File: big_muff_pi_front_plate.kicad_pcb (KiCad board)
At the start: 2 copper layers, 80 x 100 mm, 14 parts

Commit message: Finalized estetics.
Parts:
- added H11: MountingHole, MountingHole:MountingHole_3.2mm_M3_DIN965_Pad_TopBottom, F.Cu at (90.0, 145.0)
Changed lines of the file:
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@@
+		(embedded_fonts no)
+	)
+	(footprint "MountingHole:MountingHole_3.2mm_M3_DIN965_Pad_TopBottom"
+		(layer "F.Cu")
+		(at 90 145)
+		(descr "Mounting Hole 3.2mm, M3, DIN965")
+		(tags "mounting hole 3.2mm m3 din965")
+		(property "Reference" "H11"
+			(at 0 -3.8 0)
+			(layer "F.SilkS")
+			(hide yes)
+			(effects
+				(font
+					(size 1 1)
+					(thickness 0.15)
+				)
+			)
+		)
+		(property "Value" "MountingHole"
+			(at 0 3.8 0)
+			(layer "F.Fab")
+			(effects
+				(font
+					(size 1 1)
+					(thickness 0.15)
+				)
+			)
+		)
+		(property "Datasheet" ""
+			(at 0 0 0)
+			(unlocked yes)
+			(layer "F.Fab")
+			(hide yes)
+			(effects
+				(font
+					(size 1.27 1.27)
+					(thickness 0.15)
+				)
+			)
+		)
+		(property "Description" ""
+			(at 0 0 0)
+			(unlocked yes)
+			(layer "F.Fab")
+			(hide yes)
+			(effects
+				(font
+					(size 1.27 1.27)
+					(thickness 0.15)
+				)
+			)
+		)
+		(property ki_fp_filters "MountingHole*")
+		(sheetname "/")
+		(sheetfile "big_muff_pi_front_plate.kicad_sch")
+		(attr exclude_from_pos_files)
+		(fp_circle
+			(center 0 0)
+			(end 2.8 0)
+			(stroke
+				(width 0.15)
+				(type solid)
+			)
+			(fill no)
+			(layer "Cmts.User")
+		)
+		(fp_circle
+			(center 0 0)
+			(end 3.05 0)
+			(stroke
+				(width 0.05)
+				(type solid)
+			)
+			(fill no)
+			(layer "F.CrtYd")
+		)
+		(fp_text user "${REFERENCE}"
+			(at 0 0 0)
+			(layer "F.Fab")
+			(effects
+				(font
+					(size 1 1)
+					(thickness 0.15)
+				)
+			)
+		)
+		(pad "1" thru_hole circle
+			(at 0 0)
+			(size 3.6 3.6)
+			(drill 3.2)
+			(layers "*.Cu" "*.Mask")
+			(remove_unused_layers no)
+		)
+		(pad "1" connect circle
+			(at 0 0)
+			(size 5.6 5.6)
+			(layers "F.Cu" "F.Mask")
+		)
+		(pad "1" connect circle
+			(at 0 0)
+			(size 5.6 5.6)
+			(layers "B.Cu" "B.Mask")
+		)
 		(embedded_fonts no)
 	)

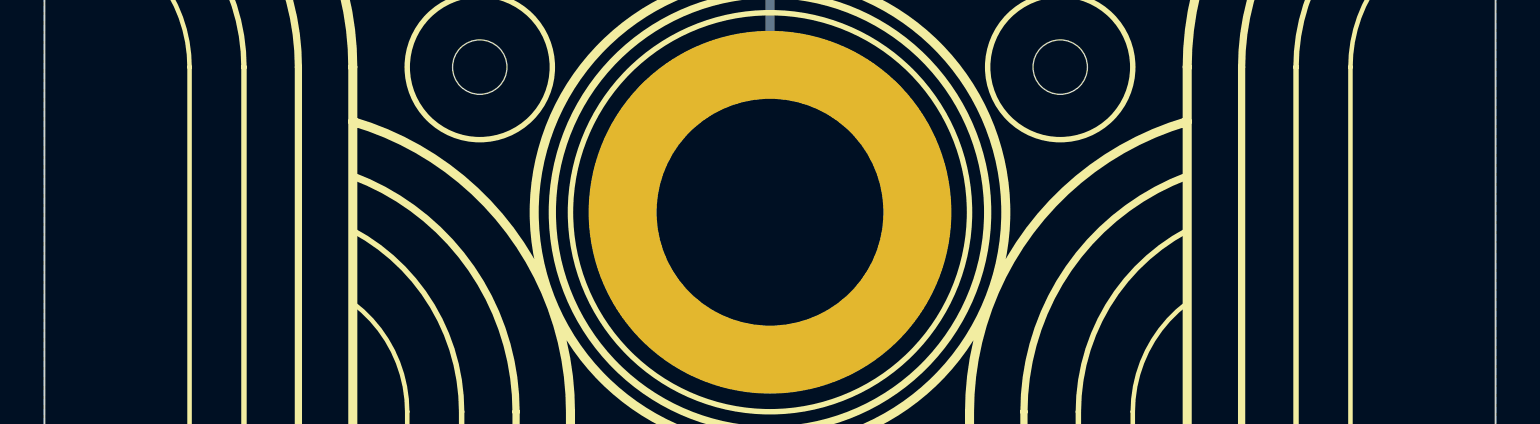
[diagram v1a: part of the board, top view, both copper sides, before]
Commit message: Added input labels.
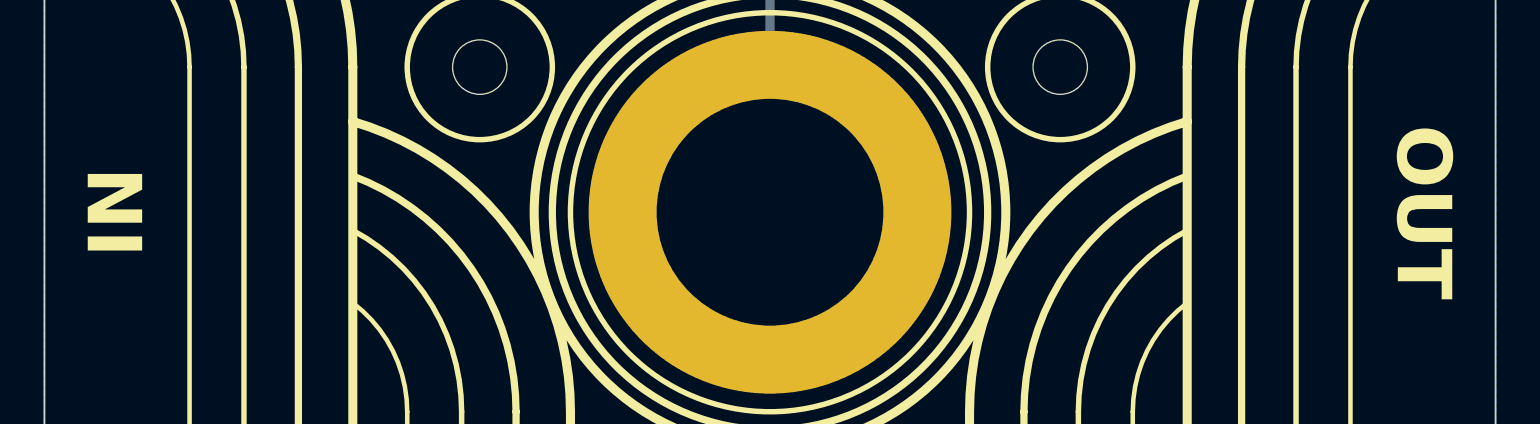
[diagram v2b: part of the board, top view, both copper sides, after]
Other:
- board text added: "IN"
- board text added: "OUT"
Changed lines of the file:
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@@
+		)
+	)
+	(gr_text "IN"
+		(at 54 125 90)
+		(layer "F.SilkS")
+		(effects
+			(font
+				(face "FreeMono")
+				(size 3 3)
+				(thickness 0.15)
+				(bold yes)
+			)
+		)
+		(render_cache "IN" 90
+			(polygon
+				(pts
+					(xy 54.822948 125.62465) (xy 54.835454 125.499793) (xy 54.867278 125.41912) (xy 54.90278 125.381321)
+					(xy 54.956045 125.356921) (xy 55.033974 125.347679) (xy 55.124784 125.364336) (xy 55.187436 125.410887)
+					(xy 55.228742 125.492234) (xy 55.245 125.62465) (xy 55.245 126.892271) (xy 55.228742 127.024687)
+					(xy 55.187436 127.106034) (xy 55.124784 127.152585) (xy 55.033974 127.169242) (xy 54.956026 127.160019)
+					(xy 54.902763 127.135674) (xy 54.867278 127.097984) (xy 54.835448 127.017154) (xy 54.822948 126.892271)
+					(xy 54.822948 126.468387) (xy 53.216807 126.468387) (xy 53.216807 126.892271) (xy 53.200549 127.024687)
+					(xy 53.159243 127.106034) (xy 53.096591 127.152585) (xy 53.005781 127.169242) (xy 52.927834 127.160019)
+					(xy 52.874571 127.135674) (xy 52.839085 127.097984) (xy 52.807255 127.017154) (xy 52.794755 126.892271)
+					(xy 52.794755 125.62465) (xy 52.807261 125.499793) (xy 52.839085 125.41912) (xy 52.874587 125.381321)
+					(xy 52.927853 125.356921) (xy 53.005781 125.347679) (xy 53.096591 125.364336) (xy 53.159243 125.410887)
+					(xy 53.200549 125.492234) (xy 53.216807 125.62465) (xy 53.216807 126.048717) (xy 54.822948 126.048717)
+				)
+			)
+			(polygon
+				(pts
+					(xy 52.794755 122.792288) (xy 52.811013 122.659872) (xy 52.852319 122.578525) (xy 52.914971 122.531974)
+					(xy 53.005781 122.515317) (xy 53.098081 122.531312) (xy 53.160648 122.575339) (xy 53.201085 122.650685)
+					(xy 53.216807 122.771405) (xy 55.245 122.771405) (xy 55.245 123.186862) (xy 53.589949 124.273865)
+					(xy 54.822948 124.273865) (xy 54.822948 124.126953) (xy 54.835454 124.002096) (xy 54.867278 123.921423)
+					(xy 54.90278 123.883624) (xy 54.956045 123.859224) (xy 55.033974 123.849982) (xy 55.124784 123.866639)
+					(xy 55.187436 123.91319) (xy 55.228742 123.994537) (xy 55.245 124.126953) (xy 55.245 124.66844)
+					(xy 55.228638 124.80323) (xy 55.187164 124.885785) (xy 55.124496 124.932838) (xy 55.033974 124.949624)
+					(xy 54.941674 124.933628) (xy 54.879107 124.889602) (xy 54.83867 124.814256) (xy 54.822948 124.693536)
+					(xy 53.216807 124.693536) (xy 53.216807 124.75655) (xy 53.200549 124.888967) (xy 53.159243 124.970313)
+					(xy 53.096591 125.016865) (xy 53.005781 125.033522) (xy 52.927834 125.024298) (xy 52.874571 124.999954)
+					(xy 52.839085 124.962264) (xy 52.807255 124.881433) (xy 52.794755 124.75655) (xy 52.794755 124.273865)
+					(xy 54.441379 123.191076) (xy 53.216807 123.191076) (xy 53.216807 123.337988) (xy 53.200549 123.470404)
+					(xy 53.159243 123.551751) (xy 53.096591 123.598302) (xy 53.005781 123.614959) (xy 52.927834 123.605736)
+					(xy 52.874571 123.581391) (xy 52.839085 123.543701) (xy 52.807255 123.462871) (xy 52.794755 123.337988)
+				)
+			)
 		)
 	)
@@
 				)
 			)
+		)
+	)
+	(gr_text "OUT\n"
+		(at 126 125 270)
+		(layer "F.SilkS")
+		(effects
+			(font
+				(face "FreeMono")
+				(size 3 3)
+				(thickness 0.15)
+				(bold yes)
+			)
+		)
+		(render_cache "OUT\n" 270
+			(polygon
+				(pts
+					(xy 126.241215 121.333826) (xy 126.475542 121.398517) (xy 126.689887 121.505071) (xy 126.887789 121.655827)
+					(xy 127.026194 121.802793) (xy 127.130639 121.957194) (xy 127.204296 122.120447) (xy 127.24874 122.294701)
+					(xy 127.263862 122.482711) (xy 127.257626 122.57863) (xy 127.236568 122.700881) (xy 127.197143 122.830729)
+					(xy 127.12098 123.000934) (xy 127.021089 123.166794) (xy 126.89823 123.315641) (xy 126.802068 123.400394)
+					(xy 126.677083 123.480345) (xy 126.517944 123.554877) (xy 126.351323 123.608616) (xy 126.166654 123.642019)
+					(xy 125.961254 123.653612) (xy 125.708975 123.631478) (xy 125.479229 123.566745) (xy 125.267445 123.459644)
+					(xy 125.070256 123.307397) (xy 124.932483 123.159644) (xy 124.828607 123.005027) (xy 124.75544 122.842155)
+					(xy 124.711358 122.66894) (xy 124.696381 122.482711) (xy 124.696396 122.482528) (xy 125.118433 122.482528)
+					(xy 125.133952 122.629592) (xy 125.179817 122.76481) (xy 125.257171 122.891376) (xy 125.369942 123.011375)
+					(xy 125.50201 123.108869) (xy 125.644375 123.177799) (xy 125.799274 123.219615) (xy 125.96968 123.233941)
+					(xy 126.146781 123.219602) (xy 126.306562 123.177924) (xy 126.452144 123.109604) (xy 126.585905 123.013573)
+					(xy 126.700543 122.894333) (xy 126.779228 122.767716) (xy 126.825962 122.631567) (xy 126.84181 122.482528)
+					(xy 126.826189 122.335682) (xy 126.779988 122.200545) (xy 126.70198 122.073906) (xy 126.588103 121.953681)
+					(xy 126.45511 121.856401) (xy 126.311423 121.787507) (xy 126.154768 121.745653) (xy 125.982137 121.731298)
+					(xy 125.807254 121.745601) (xy 125.649224 121.787214) (xy 125.504966 121.855516) (xy 125.37214 121.951666)
+					(xy 125.25858 122.070774) (xy 125.18055 122.197322) (xy 125.134169 122.333463) (xy 125.118433 122.482528)
+					(xy 124.696396 122.482528) (xy 124.711576 122.292816) (xy 124.756162 122.117463) (xy 124.829917 121.953825)
+					(xy 124.934318 121.799697) (xy 125.072454 121.653629) (xy 125.270179 121.504101) (xy 125.485091 121.398193)
+					(xy 125.720797 121.333768) (xy 125.982137 121.311628)
+				)
+			)
+			(polygon
+				(pts
+					(xy 125.615956 125.96134) (xy 125.417482 125.942676) (xy 125.243763 125.888857) (xy 125.089879 125.800737)
+					(xy 124.95247 125.675942) (xy 124.839959 125.525916) (xy 124.760696 125.365074) (xy 124.712764 125.190937)
+					(xy 124.696381 125.000184) (xy 124.712991 124.809746) (xy 124.761624 124.635767) (xy 124.842157 124.474884)
+					(xy 124.956683 124.324608) (xy 125.096185 124.19925) (xy 125.250264 124.111162) (xy 125.42201 124.057666)
+					(xy 125.615956 124.03921) (xy 126.783192 124.03921) (xy 126.802469 123.917853) (xy 126.844244 123.842367)
+					(xy 126.905971 123.798749) (xy 126.994218 123.783121) (xy 127.072165 123.792345) (xy 127.125428 123.816689)
+					(xy 127.160914 123.854379) (xy 127.192744 123.93521) (xy 127.205244 124.060093) (xy 127.205244 124.605792)
+					(xy 127.193267 124.730825) (xy 127.162929 124.811323) (xy 127.128576 124.848834) (xy 127.074974 124.873354)
+					(xy 126.994218 124.882764) (xy 126.903408 124.866107) (xy 126.840756 124.819555) (xy 126.79945 124.738209)
+					(xy 126.783192 124.605792) (xy 126.783192 124.45888) (xy 125.579685 124.45888) (xy 125.458339 124.476364)
+					(xy 125.350674 124.528254) (xy 125.252522 124.618249) (xy 125.178413 124.730822) (xy 125.133796 124.856835)
+					(xy 125.118433 125.000184) (xy 125.133804 125.143649) (xy 125.178428 125.269656) (xy 125.252522 125.382118)
+					(xy 125.350687 125.472226) (xy 125.458351 125.52417) (xy 125.579685 125.54167) (xy 126.783192 125.54167)
+					(xy 126.783192 125.394758) (xy 126.79945 125.262341) (xy 126.840756 125.180995) (xy 126.903408 125.134443)
+					(xy 126.994218 125.117787) (xy 127.072165 125.12701) (xy 127.125428 125.151354) (xy 127.160914 125.189044)
+					(xy 127.192744 125.269875) (xy 127.205244 125.394758) (xy 127.205244 125.940457) (xy 127.192569 126.068759)
+					(xy 127.160914 126.148186) (xy 127.125608 126.184686) (xy 127.072379 126.20841) (xy 126.994218 126.217429)
+					(xy 126.901918 126.201433) (xy 126.839351 126.157407) (xy 126.798914 126.082061) (xy 126.783192 125.96134)
+				)
+			)
+			(polygon
+				(pts
+					(xy 125.177051 128.000707) (xy 125.160793 128.133123) (xy 125.119487 128.21447) (xy 125.056835 128.261021)
+					(xy 124.966025 128.277678) (xy 124.875215 128.261021) (xy 124.812563 128.21447) (xy 124.771257 128.133123)
+					(xy 124.755 128.000707) (xy 124.755 127.031124) (xy 124.771257 126.898707) (xy 124.812563 126.817361)
+					(xy 124.875215 126.770809) (xy 124.966025 126.754153) (xy 125.043973 126.763376) (xy 125.097236 126.78772)
+					(xy 125.132721 126.82541) (xy 125.164551 126.906241) (xy 125.177051 127.031124) (xy 125.177051 127.303882)
+					(xy 126.783192 127.303882) (xy 126.783192 126.854903) (xy 126.392281 126.854903) (xy 126.259536 126.838685)
+					(xy 126.178094 126.797522) (xy 126.131569 126.735189) (xy 126.114944 126.644976) (xy 126.131586 126.554801)
+					(xy 126.178176 126.492466) (xy 126.259776 126.451281) (xy 126.392831 126.435049) (xy 127.205244 126.435049)
+					(xy 127.205244 128.600812) (xy 126.392831 128.600812) (xy 126.26742 128.588353) (xy 126.186385 128.556665)
+					(xy 126.148563 128.521396) (xy 126.124176 128.468481) (xy 126.114944 128.391068) (xy 126.131569 128.300855)
+					(xy 126.178094 128.238522) (xy 126.259536 128.197359) (xy 126.392281 128.181141) (xy 126.783192 128.181141)
+					(xy 126.783192 127.723552) (xy 125.177051 127.723552)
+				)
+			)
